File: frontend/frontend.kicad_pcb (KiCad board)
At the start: 2 copper layers, 32.5 x 22.5 mm, 50 parts, among them Q1 T2N7002AK,LM, Q2 NX3008PBK,215, Q3 NX3008PBK,215, Q4 T2N7002AK,LM, Q5 NX3008PBK,215, Q6 T2N7002AK,LM, U1 ADS1291/2, U2 KC2016Z2

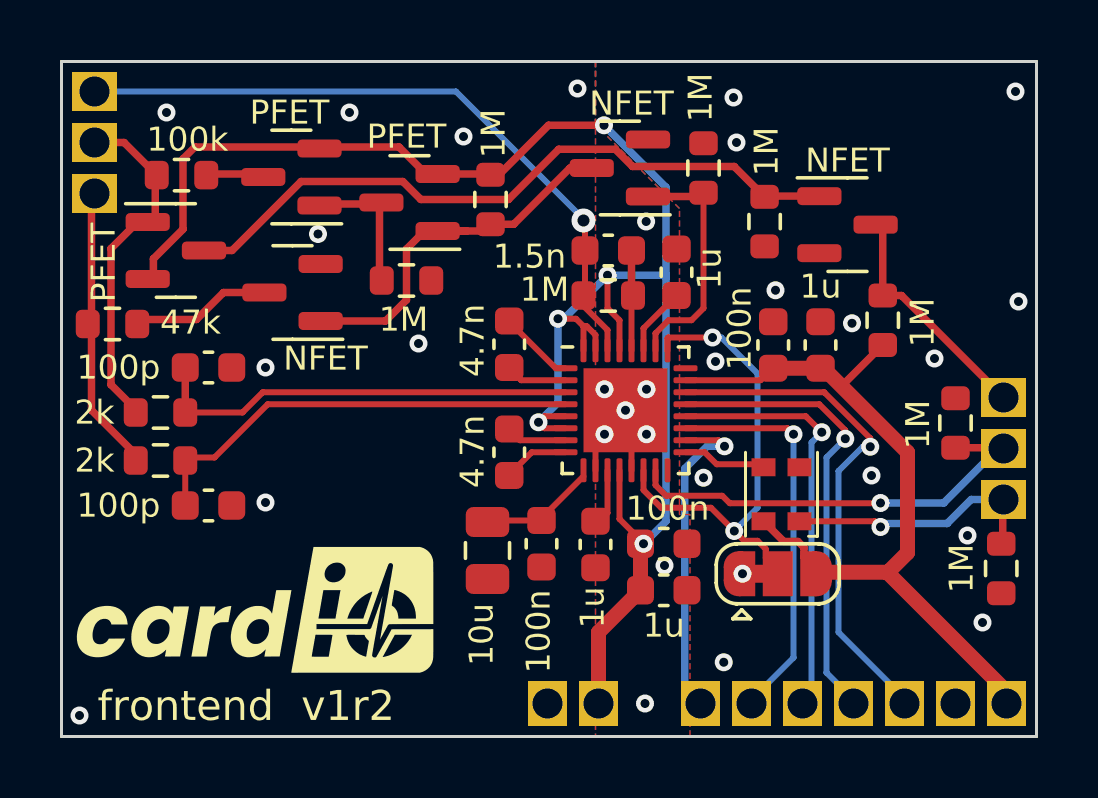
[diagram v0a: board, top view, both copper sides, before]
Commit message: Tweak frontend layout
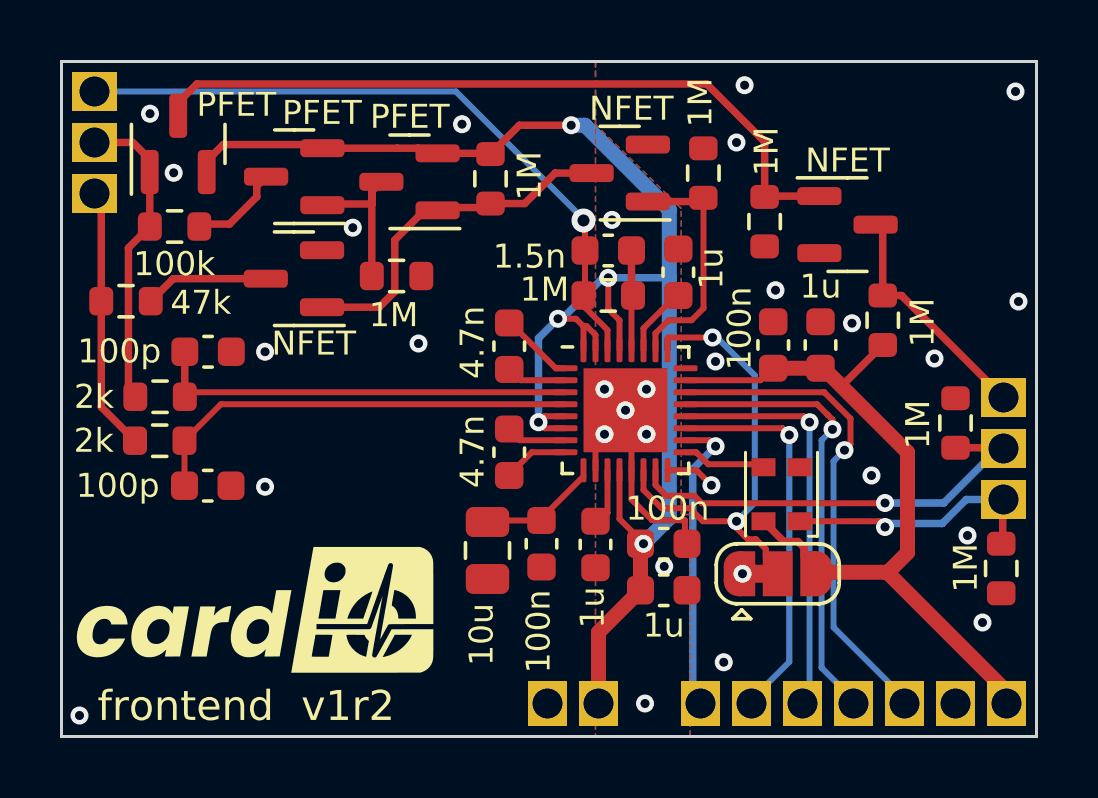
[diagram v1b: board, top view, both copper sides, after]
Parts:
- moved Q5 3.55 mm to (114.4, 63.2), turned to 90 degrees
- moved R3 1.73 mm to (114.3, 66.0)
- moved R12 0.88 mm to (112.7, 68.5)
- moved Q3 0.69 mm to (122.1, 64.5)
- moved R10 0.69 mm to (124.8, 64.4)
- moved C12 0.66 mm to (115.4, 74.6)
- moved R2 0.66 mm to (113.8, 73.1)
- moved C11 0.53 mm to (115.4, 70.2)
- moved R1 0.53 mm to (113.8, 71.7)
- moved Q4 0.46 mm to (118.2, 67.7)
- moved R9 0.36 mm to (121.7, 67.7)
- moved Q1 0.17 mm to (129.1, 64.2)
- moved R11 0.17 mm to (131.9, 64.2)
- moved Q2 0.10 mm to (118.3, 64.3)
- moved C6 0.06 mm to (125.4, 70.0)
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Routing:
- net +BATT: track 58.7 -> 52.1 mm
- net GNDA: track 2.80 -> 6.56 mm, vias 17 -> 16
- net +3.3V: track 29.2 -> 25.5 mm
- net /TOFF: track 12.8 -> 10.9 mm
- net GND: track 0.00 -> 1.67 mm
- net Net-(Q5-D): track 22.9 -> 24.2 mm
- net Net-(JP1-C): track 16.3 -> 14.9 mm
- net Net-(Q2-G): track 4.47 -> 5.76 mm
- net Net-(Q2-D): track 1.81 -> 3.08 mm
- net Net-(U1-~{CS}): track 11.0 -> 9.82 mm
- net Net-(ECG_R1-Pad1): track 9.35 -> 8.19 mm
- net Net-(Q5-G): track 11.0 -> 9.82 mm
- net Net-(U1-SCLK): track 14.1 -> 13.3 mm
- net Net-(Q4-D): track 4.72 -> 4.15 mm
- net Net-(U1-~{DRDY}): track 16.8 -> 16.3 mm

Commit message: Fix #29: fix frontend PCB pad assignment
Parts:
- ECG_L1: moved to B.Cu
- RLD_OUT1: moved to F.Cu
- moved RLD_OUT1 3.40 mm to (111.6, 64.9), turned to 0 degrees
- moved ECG_L1 1.70 mm to (111.6, 61.5), turned to 180 degrees
- moved ECG_R1 1.70 mm to (111.6, 63.2)
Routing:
- net Net-(Q5-G): track 9.82 -> 11.8 mm
- net /VGND: track 24.1 -> 25.2 mm
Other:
- board text added: "v1r3"
- board text removed: "v1r2"
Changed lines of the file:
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@@
   )
   (footprint "frontend_parts:PAD" (layer "F.Cu")
-    (at 111.6 64.9)
+    (at 111.6 63.2)
     (property "Sheetfile" "frontend.kicad_sch")
     (property "Sheetname" "")
@@
   )
   (footprint "frontend_parts:PAD" (layer "F.Cu")
+    (at 111.6 64.9)
+    (property "Sheetfile" "frontend.kicad_sch")
+    (property "Sheetname" "")
+    (attr through_hole)
+    (fp_text reference "RLD_OUT1" (at -4.3 0 unlocked) (layer "F.SilkS") hide
+        (effects (font (size 1 1) (thickness 0.15)))
+    )
+    (fp_text value "~" (at 3.81 0 unlocked) (layer "B.SilkS") hide
+        (effects (font (size 0.8 0.8) (thickness 0.1)))
+    )
+    (fp_text user "${REFERENCE}" (at 6.35 0 unlocked) (layer "F.Fab")
+        (effects (font (size 1 1) (thickness 0.15)))
+    )
+    (pad "1" thru_hole rect (at 0 0) (size 1.5 1.3) (drill 1) (layers "*.Cu" "*.Mask") (remove_unused_layers) (keep_end_layers) (zone_layer_connections)
+      (net 14 "/VGND") (pintype "passive"))
+  )
+  (footprint "frontend_parts:PAD" (layer "F.Cu")
     (at 138.6 81.9 -90)
     (property "Sheetfile" "frontend.kicad_sch")
@@
       (net 29 "Net-(U1-~{PDN}{slash}~{RESET})") (pintype "passive"))
   )
-  (footprint "frontend_parts:PAD" (layer "F.Cu")
-    (at 111.6 63.2)
-    (property "Sheetfile" "frontend.kicad_sch")
-    (property "Sheetname" "")
-    (attr through_hole)
-    (fp_text reference "ECG_L1" (at 3.81 0 unlocked) (layer "F.SilkS") hide
-        (effects (font (size 1 1) (thickness 0.1)))
-    )
-    (fp_text value "~" (at 3.81 0 unlocked) (layer "F.Fab")
-        (effects (font (size 0.8 0.8) (thickness 0.1)))
-    )
-    (fp_text user "${REFERENCE}" (at 6.35 0 unlocked) (layer "F.Fab")
-        (effects (font (size 1 1) (thickness 0.15)))
-    )
-    (pad "1" thru_hole rect (at 0 0) (size 1.5 1.3) (drill 1) (layers "*.Cu" "*.Mask") (remove_unused_layers) (keep_end_layers) (zone_layer_connections)
-      (net 16 "Net-(Q5-G)") (pintype "passive"))
-  )
   (footprint "Capacitor_SMD:C_0603_1608Metric" (layer "F.Cu")
     (at 128.3 76.6 -90)
@@
     (property "Sheetname" "")
     (attr through_hole)
-    (fp_text reference "RLD_OUT1" (at -4.3 0 unlocked) (layer "B.SilkS") hide
-        (effects (font (size 1 1) (thickness 0.15)) (justify mirror))
+    (fp_text reference "ECG_L1" (at 3.81 0 unlocked) (layer "B.SilkS") hide
+        (effects (font (size 1 1) (thickness 0.1)) (justify mirror))
     )
-    (fp_text value "~" (at 3.81 0 unlocked) (layer "F.SilkS") hide
+    (fp_text value "~" (at 3.81 0 unlocked) (layer "B.Fab")
         (effects (font (size 0.8 0.8) (thickness 0.1)) (justify mirror))
     )
@@
     )
     (pad "1" thru_hole rect (at 0 0 180) (size 1.5 1.3) (drill 1) (layers "*.Cu" "*.Mask") (remove_unused_layers) (keep_end_layers) (zone_layer_connections)
-      (net 14 "/VGND") (pintype "passive"))
+      (net 16 "Net-(Q5-G)") (pintype "passive"))
   )
   (gr_line (start 110.5 83) (end 143 83)
@@
     (effects (font (size 1 1) (thickness 0.15)) (justify left bottom))
   )
-  (gr_text "v1r2" (at 118.49 82.57) (layer "F.SilkS")
+  (gr_text "v1r3" (at 118.49 82.57) (layer "F.SilkS")
     (effects (font (size 1 1) (thickness 0.15)) (justify left bottom))
   )
@@
   (via (at 130 72.925) (size 0.6) (drill 0.3) (layers "F.Cu" "B.Cu") (net 2))
   (via (at 129.95 81.9) (size 0.6) (drill 0.3) (layers "F.Cu" "B.Cu") (free) (net 2))
-  (via (at 113.45 62.24) (size 0.6) (drill 0.3) (layers "F.Cu" "B.Cu") (free) (net 2))
+  (via (at 113.45 61.5) (size 0.6) (drill 0.3) (layers "F.Cu" "B.Cu") (free) (net 2))
   (via (at 128.85 65.78) (size 0.6) (drill 0.3) (layers "F.Cu" "B.Cu") (free) (net 2))
   (via (at 128.6 71.425) (size 0.6) (drill 0.3) (layers "F.Cu" "B.Cu") (net 2))
@@
   (segment (start 127.9 68.650707) (end 128.7 69.450707) (width 0.2) (layer "F.Cu") (net 14))
   (via (at 127.9 65.8) (size 0.8) (drill 0.4) (layers "F.Cu" "B.Cu") (net 14))
-  (segment (start 123.648529 61.5) (end 111.6 61.5) (width 0.2) (layer "B.Cu") (net 14))
+  (segment (start 111.9 64.9) (end 111.6 64.9) (width 0.2) (layer "B.Cu") (net 14))
+  (segment (start 127.9 65.751471) (end 123.948529 61.8) (width 0.2) (layer "B.Cu") (net 14))
+  (segment (start 123.948529 61.8) (end 115 61.8) (width 0.2) (layer "B.Cu") (net 14))
   (segment (start 127.9 65.8) (end 127.9 65.751471) (width 0.2) (layer "B.Cu") (net 14))
-  (segment (start 127.9 65.751471) (end 123.648529 61.5) (width 0.2) (layer "B.Cu") (net 14))
+  (segment (start 115 61.8) (end 111.9 64.9) (width 0.2) (layer "B.Cu") (net 14))
   (segment (start 129.5 68.6) (end 129.5 70.125) (width 0.2) (layer "F.Cu") (net 15))
   (segment (start 129.5 66.8) (end 129.5 68.25) (width 0.25) (layer "F.Cu") (net 15))
+  (segment (start 113.44 64.185) (end 113.44 63.74) (width 0.25) (layer "F.Cu") (net 16))
   (segment (start 112.73 66.715) (end 113.445 66) (width 0.25) (layer "F.Cu") (net 16))
-  (segment (start 111.6 63.2) (end 112.88 63.2) (width 0.25) (layer "F.Cu") (net 16))
-  (segment (start 112.88 63.2) (end 113.44 63.76) (width 0.25) (layer "F.Cu") (net 16))
   (segment (start 112.73 71.32) (end 112.73 66.715) (width 0.25) (layer "F.Cu") (net 16))
+  (segment (start 112.566116 61.5) (end 111.6 61.5) (width 0.25) (layer "F.Cu") (net 16))
+  (segment (start 113 61.933884) (end 112.566116 61.5) (width 0.25) (layer "F.Cu") (net 16))
+  (segment (start 113.44 63.74) (end 113 63.3) (width 0.25) (layer "F.Cu") (net 16))
+  (segment (start 113 63.3) (end 113 61.933884) (width 0.25) (layer "F.Cu") (net 16))
   (segment (start 112.96 71.55) (end 112.73 71.32) (width 0.25) (layer "F.Cu") (net 16))
   (segment (start 113.445 66) (end 113.445 64.19) (width 0.25) (layer "F.Cu") (net 16))
-  (segment (start 111.825 72.015) (end 111.825 65.325) (width 0.25) (layer "F.Cu") (net 17))
+  (segment (start 111.6 63.2) (end 111.85 63.2) (width 0.25) (layer "F.Cu") (net 17))
+  (segment (start 111.85 63.2) (end 112.72 64.07) (width 0.25) (layer "F.Cu") (net 17))
+  (segment (start 112.72 66.088604) (end 111.825 66.983604) (width 0.25) (layer "F.Cu") (net 17))
   (segment (start 112.885 73.075) (end 111.825 72.015) (width 0.25) (layer "F.Cu") (net 17))
+  (segment (start 111.825 66.983604) (end 111.825 68.49) (width 0.25) (layer "F.Cu") (net 17))
+  (segment (start 112.72 64.07) (end 112.72 66.088604) (width 0.25) (layer "F.Cu") (net 17))
   (segment (start 133.000498 76.050498) (end 133.000498 75.8245) (width 0.2) (layer "F.Cu") (net 18))
   (segment (start 131.445685 75.39) (end 130.504339 75.39) (width 0.2) (layer "F.Cu") (net 18))

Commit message: Update no-bom metadata
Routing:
- net Net-(ECG_R1-Pad1): track 7.77 -> 11.3 mm
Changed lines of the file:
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@@
     (property "Sheetfile" "frontend.kicad_sch")
     (property "Sheetname" "")
-    (attr through_hole)
+    (property "exclude_from_bom" "")
+    (attr through_hole exclude_from_bom)
     (fp_text reference "MISO1" (at 3.81 0 -90 unlocked) (layer "F.SilkS") hide
         (effects (font (size 1 1) (thickness 0.1)))
@@
     (property "Sheetfile" "frontend.kicad_sch")
     (property "Sheetname" "")
-    (attr through_hole)
+    (property "exclude_from_bom" "")
+    (attr through_hole exclude_from_bom)
     (fp_text reference "DGND1" (at 3.81 0 90 unlocked) (layer "F.SilkS") hide
         (effects (font (size 1 1) (thickness 0.1)))
@@
     (property "Sheetfile" "frontend.kicad_sch")
     (property "Sheetname" "")
-    (attr through_hole)
+    (property "exclude_from_bom" "")
+    (attr through_hole exclude_from_bom)
     (fp_text reference "ECG_R1" (at 3.81 0 unlocked) (layer "F.SilkS") hide
         (effects (font (size 1 1) (thickness 0.1)))
@@
     (property "Sheetfile" "frontend.kicad_sch")
     (property "Sheetname" "")
-    (attr through_hole)
+    (property "exclude_from_bom" "")
+    (attr through_hole exclude_from_bom)
     (fp_text reference "~{TOUCH_DET}1" (at 3.81 0 unlocked) (layer "F.SilkS") hide
         (effects (font (size 1 1) (thickness 0.1)))
@@
     (property "Sheetfile" "frontend.kicad_sch")
     (property "Sheetname" "")
-    (attr through_hole)
+    (property "exclude_from_bom" "")
+    (attr through_hole exclude_from_bom)
     (fp_text reference "CLK_EN1" (at -3.8 0.1 unlocked) (layer "B.SilkS") hide
         (effects (font (size 1 1) (thickness 0.15)) (justify mirror))
@@
     (property "Sheetfile" "frontend.kicad_sch")
     (property "Sheetname" "")
-    (attr through_hole)
+    (property "exclude_from_bom" "")
+    (attr through_hole exclude_from_bom)
     (fp_text reference "MOSI1" (at 3.81 0 -90 unlocked) (layer "F.SilkS") hide
         (effects (font (size 1 1) (thickness 0.1)))
@@
     (property "Sheetfile" "frontend.kicad_sch")
     (property "Sheetname" "")
+    (property "exclude_from_bom" "")
     (property "ki_description" "3-pole Solder Jumper, pins 1+2 closed/bridged")
     (property "ki_keywords" "Solder Jumper SPDT")
-    (attr exclude_from_pos_files)
+    (attr exclude_from_pos_files exclude_from_bom)
     (net_tie_pad_groups "1, 2, 3")
     (fp_text reference "JP1" (at 0 -1.8) (layer "F.SilkS") hide
@@
     (property "Sheetfile" "frontend.kicad_sch")
     (property "Sheetname" "")
-    (attr through_hole)
+    (property "exclude_from_bom" "")
+    (attr through_hole exclude_from_bom)
     (fp_text reference "AVSS1" (at 3.81 0 90 unlocked) (layer "F.SilkS") hide
         (effects (font (size 1 1) (thickness 0.1)))
@@
     (property "Sheetfile" "frontend.kicad_sch")
     (property "Sheetname" "")
-    (attr smd)
+    (property "exclude_from_bom" "")
+    (attr smd exclude_from_bom)
     (fp_text reference "G1" (at -0.25 2.95 unlocked) (layer "F.SilkS") hide
         (effects (font (size 1 1) (thickness 0.1)))
@@
     (property "Sheetfile" "frontend.kicad_sch")
     (property "Sheetname" "")
-    (attr through_hole)
+    (property "exclude_from_bom" "")
+    (attr through_hole exclude_from_bom)
     (fp_text reference "SCLK1" (at 3.81 0 -90 unlocked) (layer "F.SilkS") hide
         (effects (font (size 1 1) (thickness 0.1)))
@@
     (property "Sheetfile" "frontend.kicad_sch")
     (property "Sheetname" "")
-    (attr through_hole)
+    (property "exclude_from_bom" "")
+    (attr through_hole exclude_from_bom)
     (fp_text reference "RLD_OUT1" (at -4.3 0 unlocked) (layer "F.SilkS") hide
         (effects (font (size 1 1) (thickness 0.15)))
@@
     (property "Sheetfile" "frontend.kicad_sch")
     (property "Sheetname" "")
-    (attr through_hole)
+    (property "exclude_from_bom" "")
+    (attr through_hole exclude_from_bom)
     (fp_text reference locked "~{DRDY}1" (at 3.81 0 -90 unlocked) (layer "F.SilkS") hide
         (effects (font (size 1 1) (thickness 0.1)))
@@
     (property "Sheetfile" "frontend.kicad_sch")
     (property "Sheetname" "")
-    (attr through_hole)
+    (property "exclude_from_bom" "")
+    (attr through_hole exclude_from_bom)
     (fp_text reference "AVDD1" (at 3.81 0 90 unlocked) (layer "F.SilkS") hide
         (effects (font (size 1 1) (thickness 0.1)))
@@
     (property "Sheetfile" "frontend.kicad_sch")
     (property "Sheetname" "")
-    (attr through_hole)
+    (property "exclude_from_bom" "")
+    (attr through_hole exclude_from_bom)
     (fp_text reference "~{CS}1" (at 3.81 0 -90 unlocked) (layer "F.SilkS") hide
         (effects (font (size 1 1) (thickness 0.1)))
@@
     (property "Sheetfile" "frontend.kicad_sch")
     (property "Sheetname" "")
-    (attr through_hole)
+    (property "exclude_from_bom" "")
+    (attr through_hole exclude_from_bom)
     (fp_text reference "~{RESET}/~{PDN}1" (at 3.81 0 unlocked) (layer "F.SilkS") hide
         (effects (font (size 1 1) (thickness 0.1)))
@@
     (property "Sheetfile" "frontend.kicad_sch")
     (property "Sheetname" "")
-    (attr through_hole)
+    (property "exclude_from_bom" "")
+    (attr through_hole exclude_from_bom)
     (fp_text reference "DVDD1" (at 3.81 0 90 unlocked) (layer "F.SilkS") hide
         (effects (font (size 1 1) (thickness 0.1)))
@@
     (property "Sheetfile" "frontend.kicad_sch")
     (property "Sheetname" "")
-    (attr through_hole)
+    (property "exclude_from_bom" "")
+    (attr through_hole exclude_from_bom)
     (fp_text reference "ECG_L1" (at 3.81 0 unlocked) (layer "B.SilkS") hide
         (effects (font (size 1 1) (thickness 0.1)) (justify mirror))
@@
   (segment (start 112.72 66.088604) (end 111.825 66.983604) (width 0.25) (layer "F.Cu") (net 17))
   (segment (start 112.885 73.075) (end 111.825 72.015) (width 0.25) (layer "F.Cu") (net 17))
+  (segment (start 111.825 72.015) (end 111.825 68.49) (width 0.25) (layer "F.Cu") (net 17))
   (segment (start 111.825 66.983604) (end 111.825 68.49) (width 0.25) (layer "F.Cu") (net 17))
   (segment (start 112.72 64.07) (end 112.72 66.088604) (width 0.25) (layer "F.Cu") (net 17))
